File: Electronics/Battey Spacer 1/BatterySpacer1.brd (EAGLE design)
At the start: 30 x 30 mm, 0 parts

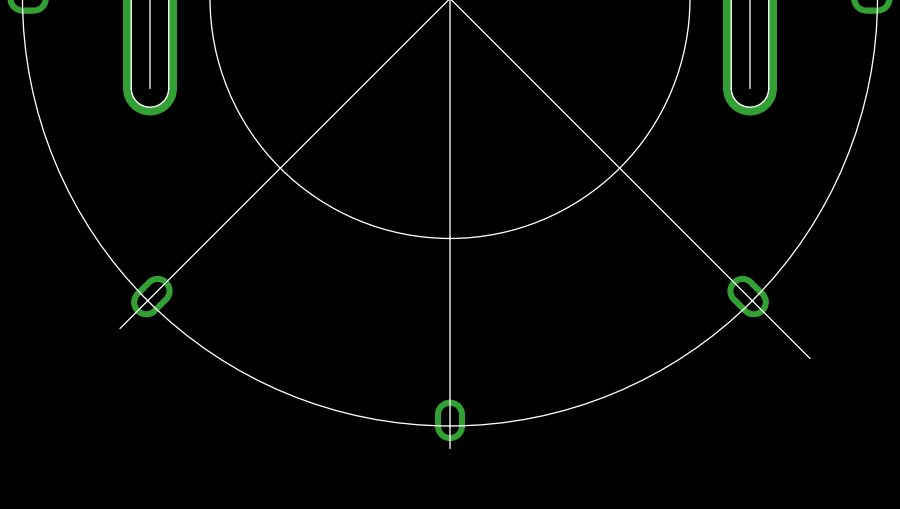
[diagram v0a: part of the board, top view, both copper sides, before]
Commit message: Electronics start, GPS code
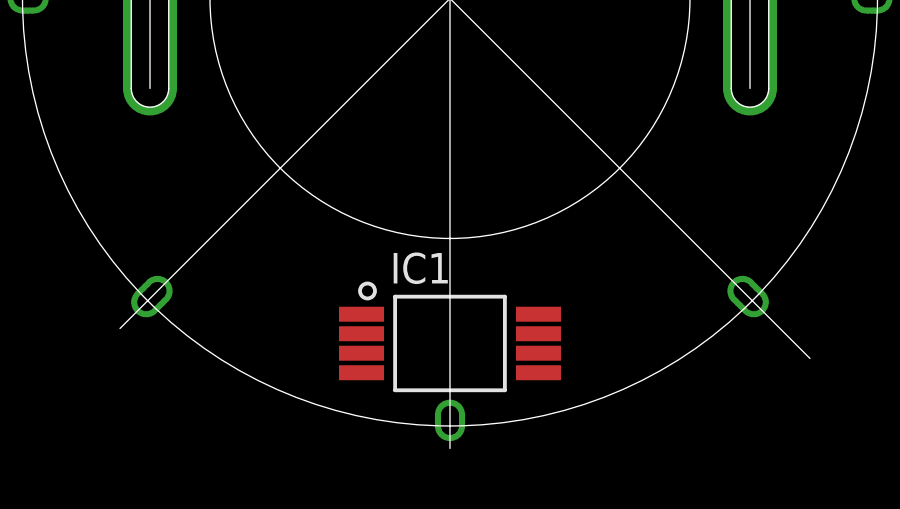
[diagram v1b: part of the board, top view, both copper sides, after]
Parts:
- added IC1: MCP9843T, MarkIIEaglelbr:TSSOP
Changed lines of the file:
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@@
 </autorouter>
 <elements>
+<element name="IC1" library="MarkIIEaglelbr" package="TSSOP" value="MCP9843T" x="14" y="2.5"/>
 </elements>
 <signals>
